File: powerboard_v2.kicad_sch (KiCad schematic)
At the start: 25 parts, among them J1 Conn_01x02_Pin, J2 Conn_01x02_Pin, J3 Conn_01x02_Pin, J7 Conn_01x04_Socket, J8 Conn_ST_STDC14, SW1 SW_Wuerth_450301014042, SW2 SW_Push, U1 STM32F303K8Tx, U2 BD33FC0FP, U3 MCP2562-E-P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

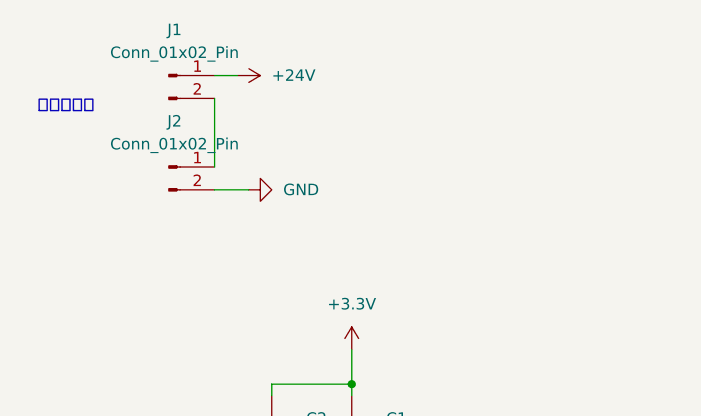
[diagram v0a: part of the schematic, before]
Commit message: くそでかコンデンサを配置
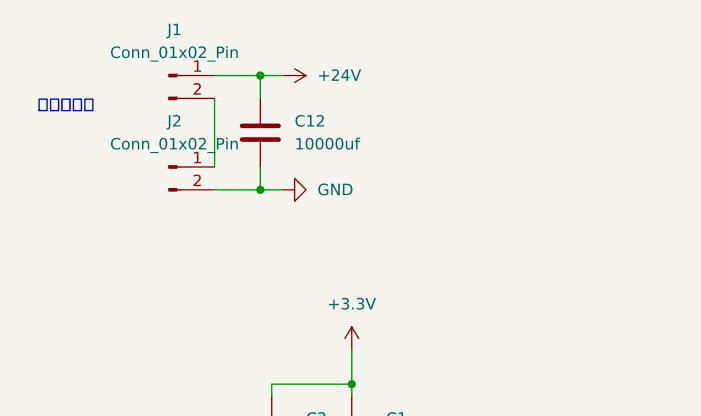
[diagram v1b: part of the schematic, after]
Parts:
- added C12: 10000uf, symbol Device:C
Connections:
- net +24V: now also C12.1
- net GND: now also C12.2
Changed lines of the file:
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@@
 	)
 	(junction
+		(at 40.64 33.02)
+		(diameter 0)
+		(color 0 0 0 0)
+	)
+	(junction
+		(at 40.64 20.32)
+		(diameter 0)
+		(color 0 0 0 0)
+	)
+	(junction
 		(at 63.5 165.1)
 		(diameter 0)
@@
 	(wire
 		(pts
+			(xy 40.64 30.48) (xy 40.64 33.02)
+		)
+		(stroke
+			(width 0)
+			(type default)
+		)
+	)
+	(wire
+		(pts
 			(xy 87.63 165.1) (xy 87.63 157.48)
 		)
@@
 	(wire
 		(pts
+			(xy 40.64 20.32) (xy 40.64 22.86)
+		)
+		(stroke
+			(width 0)
+			(type default)
+		)
+	)
+	(wire
+		(pts
 			(xy 63.5 166.37) (xy 63.5 165.1)
 		)
@@
 	(wire
 		(pts
-			(xy 35.56 20.32) (xy 38.1 20.32)
+			(xy 35.56 20.32) (xy 40.64 20.32)
 		)
 		(stroke
@@
 	(wire
 		(pts
+			(xy 40.64 20.32) (xy 43.18 20.32)
+		)
+		(stroke
+			(width 0)
+			(type default)
+		)
+	)
+	(wire
+		(pts
 			(xy 125.73 113.03) (xy 127 113.03)
 		)
@@
 	(wire
 		(pts
+			(xy 40.64 33.02) (xy 35.56 33.02)
+		)
+		(stroke
+			(width 0)
+			(type default)
+		)
+	)
+	(wire
+		(pts
 			(xy 50.8 66.04) (xy 52.07 66.04)
 		)
@@
 	(wire
 		(pts
-			(xy 39.37 33.02) (xy 35.56 33.02)
+			(xy 43.18 33.02) (xy 40.64 33.02)
 		)
 		(stroke
@@
 	(symbol
 		(lib_id "power:GND")
-		(at 39.37 33.02 90)
+		(at 43.18 33.02 90)
 		(unit 1)
 		(exclude_from_sim no)
@@
 		(fields_autoplaced yes)
 		(property "Reference" "#PWR01"
-			(at 45.72 33.02 0)
+			(at 49.53 33.02 0)
 			(effects
 				(font
@@
 		)
 		(property "Value" "GND"
-			(at 43.18 33.0199 90)
+			(at 46.99 33.0199 90)
 			(effects
 				(font
@@
 		)
 		(property "Footprint" ""
-			(at 39.37 33.02 0)
+			(at 43.18 33.02 0)
 			(effects
 				(font
@@
 		)
 		(property "Datasheet" ""
-			(at 39.37 33.02 0)
+			(at 43.18 33.02 0)
 			(effects
 				(font
@@
 		)
 		(property "Description" "Power symbol creates a global label with name \"GND\" , ground"
-			(at 39.37 33.02 0)
+			(at 43.18 33.02 0)
 			(effects
 				(font
@@
 	(symbol
 		(lib_id "power:+24V")
-		(at 38.1 20.32 270)
+		(at 43.18 20.32 270)
 		(unit 1)
 		(exclude_from_sim no)
@@
 		(fields_autoplaced yes)
 		(property "Reference" "#PWR02"
-			(at 34.29 20.32 0)
+			(at 39.37 20.32 0)
 			(effects
 				(font
@@
 		)
 		(property "Value" "+24V"
-			(at 41.91 20.3199 90)
+			(at 46.99 20.3199 90)
 			(effects
 				(font
@@
 		)
 		(property "Footprint" ""
-			(at 38.1 20.32 0)
+			(at 43.18 20.32 0)
 			(effects
 				(font
@@
 		)
 		(property "Datasheet" ""
-			(at 38.1 20.32 0)
+			(at 43.18 20.32 0)
 			(effects
 				(font
@@
 		)
 		(property "Description" "Power symbol creates a global label with name \"+24V\""
-			(at 38.1 20.32 0)
+			(at 43.18 20.32 0)
 			(effects
 				(font
@@
 					(unit 1)
 				)
+			)
+		)
+	)
+	(symbol
+		(lib_id "Device:C")
+		(at 40.64 26.67 0)
+		(unit 1)
+		(exclude_from_sim no)
+		(in_bom yes)
+		(on_board yes)
+		(dnp no)
+		(fields_autoplaced yes)
+		(property "Reference" "C12"
+			(at 44.45 25.3999 0)
+			(effects
+				(font
+					(size 1.27 1.27)
+				)
+				(justify left)
+			)
+		)
+		(property "Value" "10000uf"
+			(at 44.45 27.9399 0)
+			(effects
+				(font
+					(size 1.27 1.27)
+				)
+				(justify left)
+			)
+		)
+		(property "Footprint" ""
+			(at 41.6052 30.48 0)
+			(effects
+				(font
+					(size 1.27 1.27)
+				)
+				(hide yes)
+			)
+		)
+		(property "Datasheet" "~"
+			(at 40.64 26.67 0)
+			(effects
+				(font
+					(size 1.27 1.27)
+				)
+				(hide yes)
+			)
+		)
+		(property "Description" "Unpolarized capacitor"
+			(at 40.64 26.67 0)
+			(effects
+				(font
+					(size 1.27 1.27)
+				)
+				(hide yes)
+			)
+		)
+		(pin "1"
+		)
+		(pin "2"
+		)
+		(instances
+			(project ""
+				(path "/6e0ca105-c789-4be3-8f3a-c5e169be0bfe"
+					(reference "C12")
+					(unit 1)
+				)

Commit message: 一応バックアップ
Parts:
- added C13: 0.1uf, symbol Device:C
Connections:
- net +3.3V: now also C13.1
- net GND: no longer C12.2, J2.2 (Pin_2)
- net at U1.5 (VDDA): now also C13.2
- new net GND2: C12.2, J2.2 (Pin_2)
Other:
- note removed: "駆動用電源"
- moved on the sheet: C1, C10, C11, C2, C3, C4, C5, C6, C7, C8, C9, D1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
